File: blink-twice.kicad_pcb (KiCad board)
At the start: 2 copper layers, 38.2 x 27 mm, 13 parts, among them U2 4017, U3 NE555P

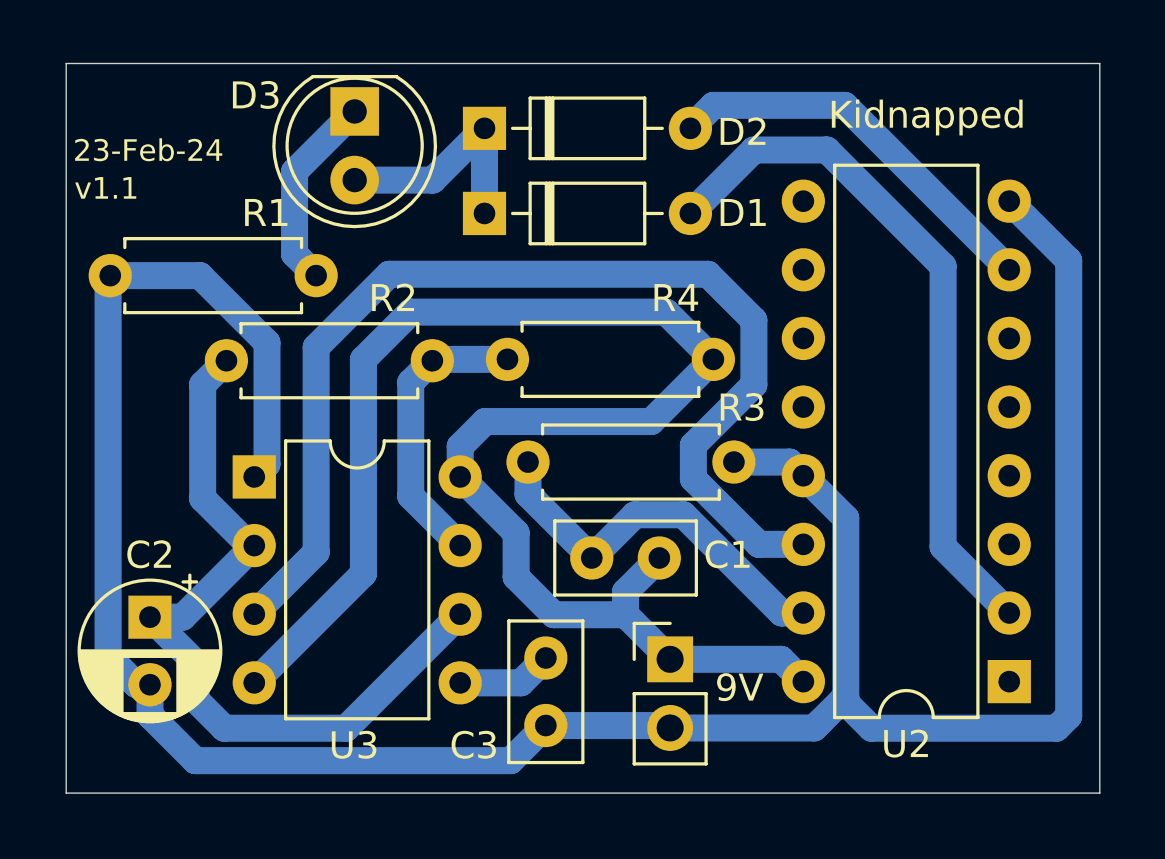
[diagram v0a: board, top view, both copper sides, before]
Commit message: Groomed, and saved with KiCad 8.
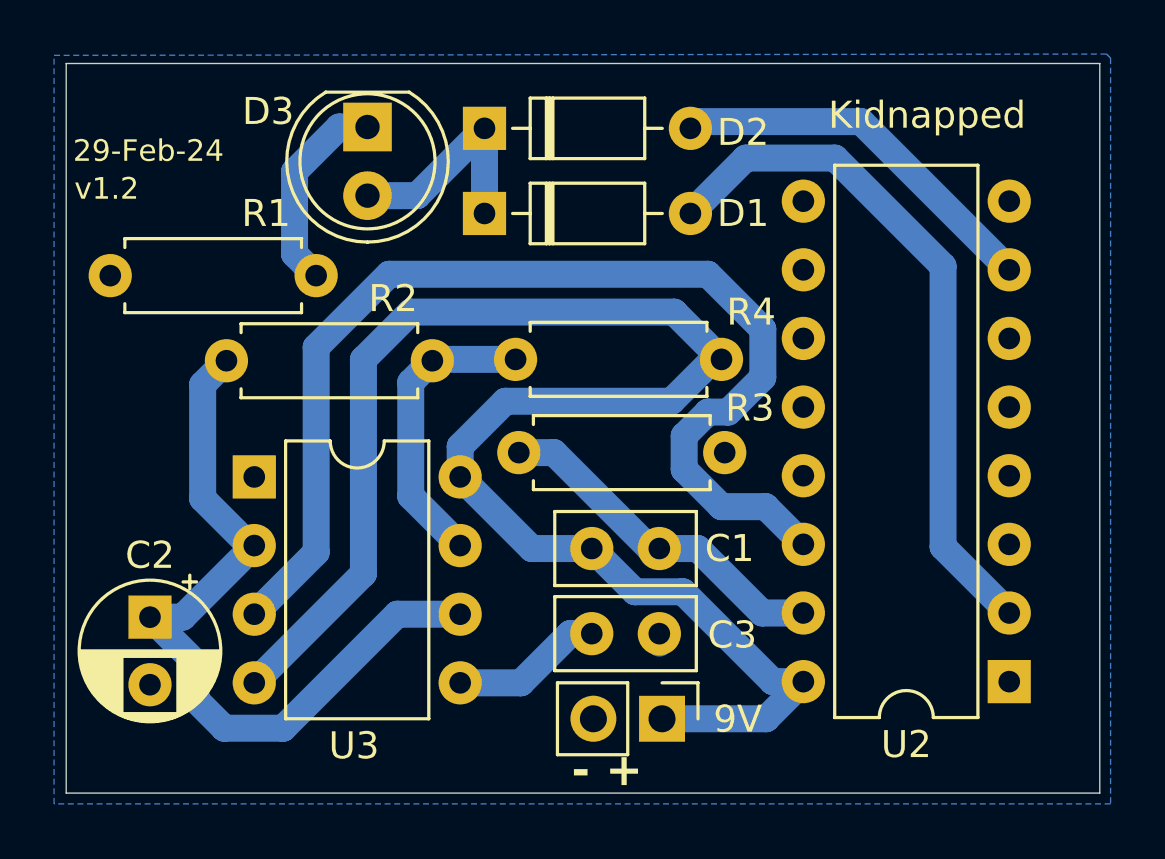
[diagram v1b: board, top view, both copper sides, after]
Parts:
- moved C1 2.52 mm to (148.4, 107.3), turned to 0 degrees
- moved BT1 2.22 mm to (151.0, 113.6), turned to -90 degrees
- moved C3 1.92 mm to (148.4, 110.5), turned to 0 degrees
- moved D3 0.75 mm to (140.1, 91.7)
- moved R4 0.49 mm to (145.7, 103.8)
- moved R3 0.30 mm to (153.2, 100.3)
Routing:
- net GND: track 97.3 -> 0.71 mm
- net Net-(BT1-+): track 59.9 -> 62.1 mm
- net Net-(U3-CV): track 3.55 -> 5.62 mm
- net Net-(U2-Reset): track 14.5 -> 13.0 mm
- net Net-(U2-CLK): track 40.7 -> 41.7 mm
- added copper zone on B.Cu, net GND
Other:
- board text added: "- +"
- board text added: "29-Feb-24"
- board text added: "v1.2"
- board text removed: "23-Feb-24"
- board text removed: "v1.1"
